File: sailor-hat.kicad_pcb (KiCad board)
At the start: 4 copper layers, 65 x 56 mm, 119 parts, among them J501 Screw_Terminal_01x03, J601 Conn_02x07_Counter_Clockwise, J701 Screw_Terminal_01x02, J702 Raspberry_Pi_2_3, J801 Screw_Terminal_01x04, Q501 WST03P06, SW201 SW_SPST, U201 TPS61022, U301 H7533-H#, U302 TX4138, U303 INA199A1DCKR, U401 DS3231MZ, U601 ATtiny841-SSU, U701 RCLAMP0524P-N, U801 RCLAMP0524P-N, U802 H7550-H#, U803 MCP2515-xST, U804 ISO1050DUB, Y801 1C208000CE0Q

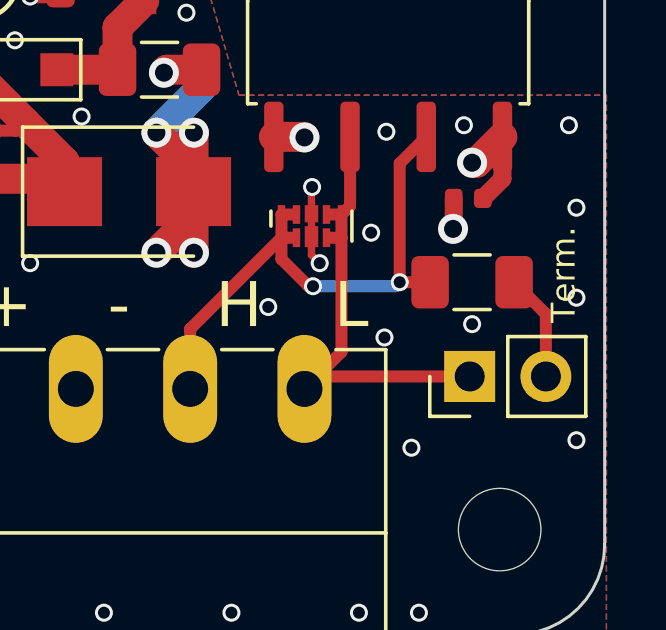
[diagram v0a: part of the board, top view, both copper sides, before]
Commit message: Change CAN termination jumper to a solder jumper
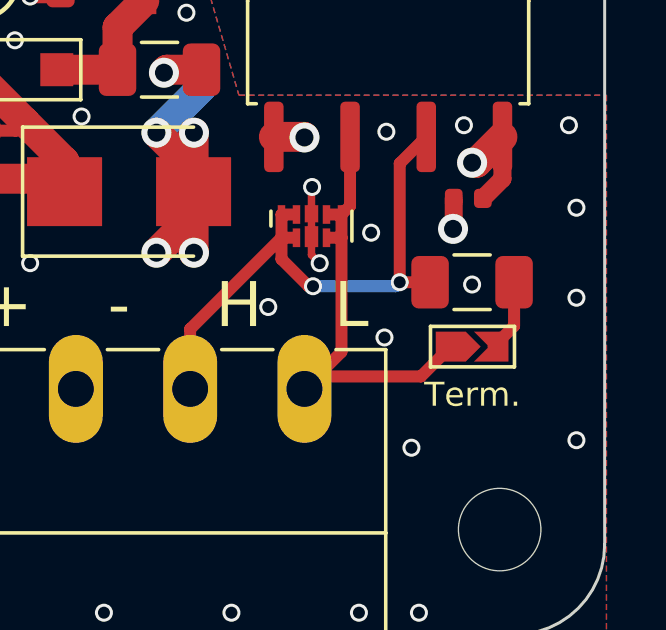
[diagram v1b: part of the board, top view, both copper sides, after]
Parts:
- JP801: footprint Connector_PinHeader_2.54mm:PinHeader_1x02_P2.54mm_Vertical -> custom:SolderJumper-2_P1.3mm_Open_TrianglePad_Narrow
- moved JP801 1.00 mm to (80.8, 64.6), turned to 0 degrees
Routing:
- net Net-(JP801-Pad2): track 3.58 -> 2.43 mm
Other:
- board text added: "CR1220"
- board text removed: "CR1220 battery"

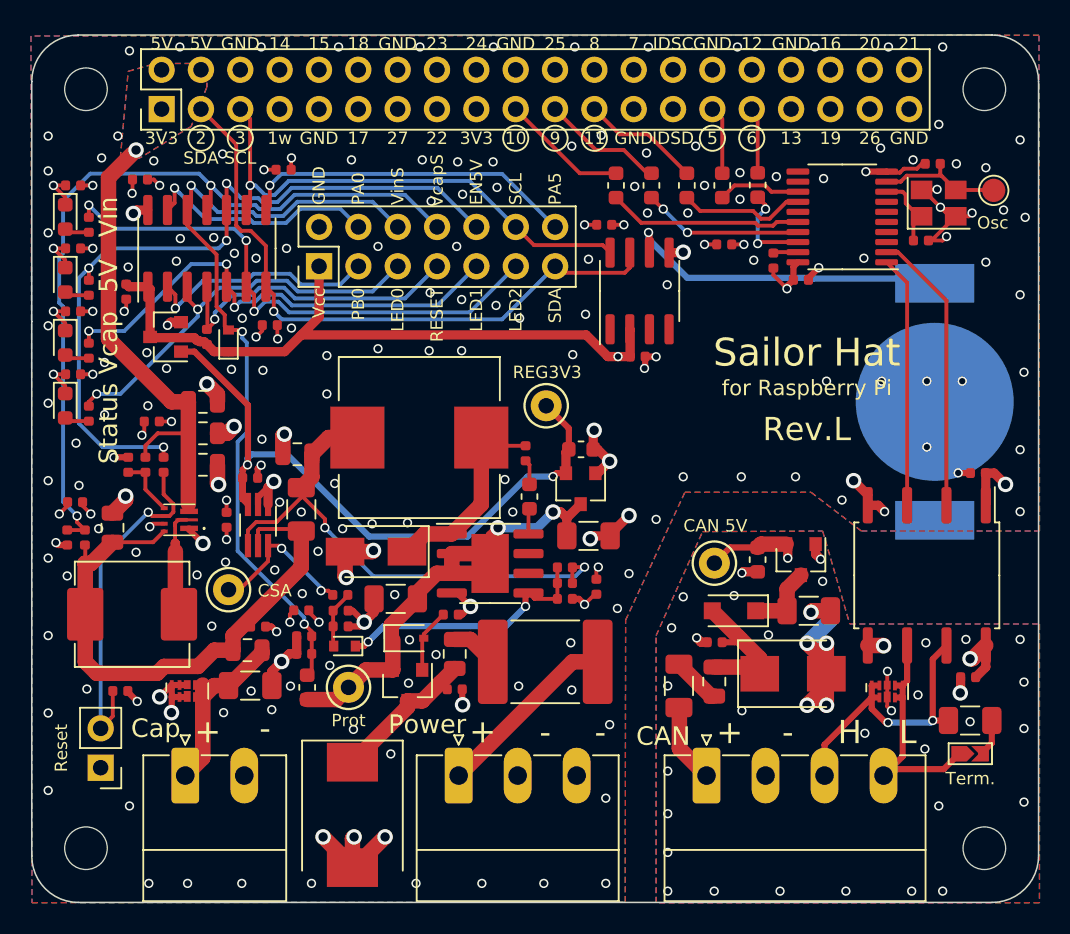
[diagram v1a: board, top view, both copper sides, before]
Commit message: Flipped the battery to the top side of the board
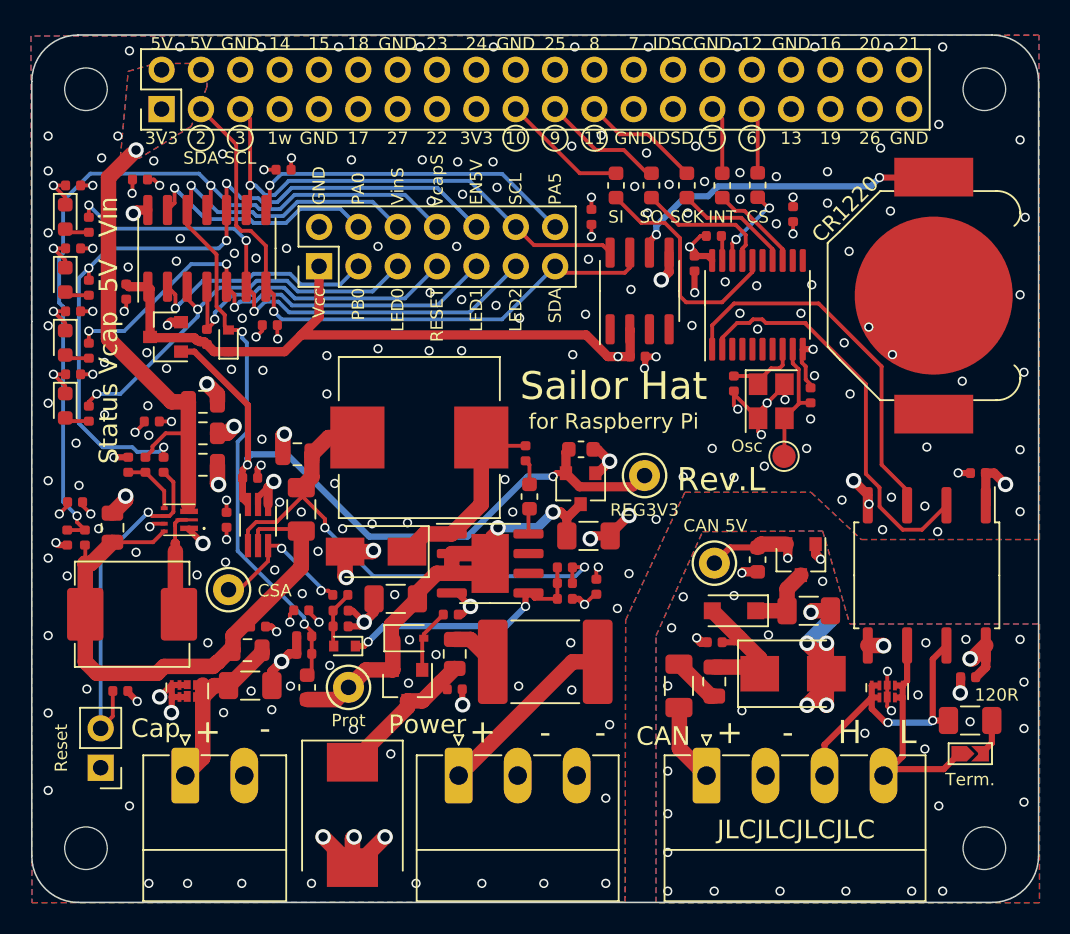
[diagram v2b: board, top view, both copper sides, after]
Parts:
- BT401: moved to F.Cu
- moved TP801 21.9 mm to (68.8, 45.4), turned to 270 degrees
- moved C804 16.9 mm to (70.5, 41.5), turned to 90 degrees
- moved Y801 16.7 mm to (67.9, 41.9), turned to 270 degrees
- moved C803 15.2 mm to (65.5, 40.7), turned to 270 degrees
- moved U803 7.89 mm to (67.0, 35.6), turned to 90 degrees
- moved TP301 7.79 mm to (59.8, 46.7)
- moved C806 6.95 mm to (63.0, 33.0), turned to 270 degrees
- moved BT401 6.86 mm to (78.4, 35.1), turned to 90 degrees
- moved C906 4.86 mm to (69.3, 29.8), turned to 270 degrees
- moved R802 4.16 mm to (64.2, 31.2), turned to 0 degrees
- moved C909 0.97 mm to (56.3, 30.0), turned to 90 degrees
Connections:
- BT401 pad 1: /RTC/VBAT -> (no net)
- BT401 pad 2: (no net) -> /RTC/VBAT
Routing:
- net /CANbus interface/CAN_TX: track 16.2 -> 24.4 mm
- net /CANbus interface/CAN_RX: track 18.4 -> 26.2 mm
- net /SI: track 12.6 -> 15.4 mm
- net REG3.3V: track 43.8 -> 46.2 mm
- net GND: track 93.5 -> 91.8 mm, vias 205 -> 217
- net /SO: track 10.4 -> 8.88 mm, vias 2 -> 0
- net /INT0: track 5.38 -> 6.01 mm
- net /CS0: track 6.05 -> 5.51 mm
- net /SCK: track 8.19 -> 7.65 mm
- net +3V3: track 20.2 -> 19.7 mm
- net /RTC/VBAT: track 21.6 -> 21.1 mm, vias 1 -> 2
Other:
- net class Default: clearance 0.2 -> 0.127
- net class Power: clearance 0.2 -> 0.127
- rule trace_clearance: 0.2 -> 0.127
- board text added: "120R"
- board text added: "CS"
- board text added: "INT"
- board text added: "JLCJLCJLCJLC"
- board text added: "SCK"
- board text added: "SI"
- board text added: "SO"

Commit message: Make power connector identical to SH-ESP32 for consistency
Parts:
- J501: value Screw_Terminal_01x03 -> Screw_Terminal_01x02; footprint Connector_Phoenix_MC:PhoenixContact_MC_1,5_3-G-3.81_1x03_P3.81mm_Horizontal -> Connector_Phoenix_MC:PhoenixContact_MC_1,5_2-G-3.81_1x02_P3.81mm_Horizontal
- J701: value Screw_Terminal_01x02 -> Screw_Terminal_01x03; footprint Connector_Phoenix_MC:PhoenixContact_MC_1,5_2-G-3.81_1x02_P3.81mm_Horizontal -> Connector_Phoenix_MC:PhoenixContact_MC_1,5_3-G-3.81_1x03_P3.81mm_Horizontal
- moved J501 3.75 mm to (51.5, 66.0)
- moved D501 3.68 mm to (44.6, 68.6)
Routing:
- net /Protection/Vin: track 12.0 -> 9.47 mm
- net /Protection/Vin_fused: track 9.96 -> 8.54 mm
- net GND: vias 217 -> 219
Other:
- board text removed: "120R"
